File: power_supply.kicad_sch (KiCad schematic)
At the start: 0 parts

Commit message: add library from macbook
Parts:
- added U1: BQ25713RSNR, RSN0032B, symbol 2025-10-10_18-15-19:BQ25713RSNR
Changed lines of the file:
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@@
 	(generator_version "9.0")
 	(paper "A4")
+	(symbol
+		(lib_id "2025-10-10_18-15-19:BQ25713RSNR")
+		(at 91.44 86.36 0)
+		(unit 1)
+		(exclude_from_sim no)
+		(in_bom yes)
+		(on_board yes)
+		(dnp no)
+		(fields_autoplaced yes)
+		(property "Reference" "U1"
+			(at 91.44 30.48 0)
+			(effects
+				(font
+					(size 1.524 1.524)
+				)
+			)
+		)
+		(property "Value" "BQ25713RSNR"
+			(at 91.44 33.02 0)
+			(effects
+				(font
+					(size 1.524 1.524)
+				)
+			)
+		)
+		(property "Footprint" "RSN0032B"
+			(at 91.44 86.36 0)
+			(effects
+				(font
+					(size 1.27 1.27)
+					(italic yes)
+				)
+				(hide yes)
+			)
+		)
+		(property "Datasheet" "https://www.ti.com/lit/gpn/bq25713"
+			(at 91.44 86.36 0)
+			(effects
+				(font
+					(size 1.27 1.27)
+					(italic yes)
+				)
+				(hide yes)
+			)
+		)
+		(property "Description" ""
+			(at 91.44 86.36 0)
+			(effects
+				(font
+					(size 1.27 1.27)
+				)
+				(hide yes)
+			)
+		)
+		(pin "8"
+		)
+		(pin "9"
+		)
+		(pin "10"
+		)
+		(pin "27"
+		)
+		(pin "6"
+		)
+		(pin "28"
+		)
+		(pin "17"
+		)
+		(pin "18"
+		)
+		(pin "33"
+		)
+		(pin "32"
+		)
+		(pin "13"
+		)
+		(pin "12"
+		)
+		(pin "4"
+		)
+		(pin "5"
+		)
+		(pin "15"
+		)
+		(pin "14"
+		)
+		(pin "25"
+		)
+		(pin "23"
+		)
+		(pin "26"
+		)
+		(pin "24"
+		)
+		(pin "22"
+		)
+		(pin "21"
+		)
+		(pin "20"
+		)
+		(pin "19"
+		)
+		(pin "29"
+		)
+		(pin "30"
+		)
+		(pin "1"
+		)
+		(pin "11"
+		)
+		(pin "2"
+		)
+		(pin "3"
+		)
+		(pin "16"
+		)
+		(pin "7"
+		)
+		(pin "31"
+		)
+		(instances
+			(project ""
+				(path "/6a10ea30-147f-4e88-a5c3-bf0fd41178aa/90f8a919-9308-4e2d-9785-824a1b667211"
+					(reference "U1")
+					(unit 1)
+				)
+			)
+		)
+	)
 )

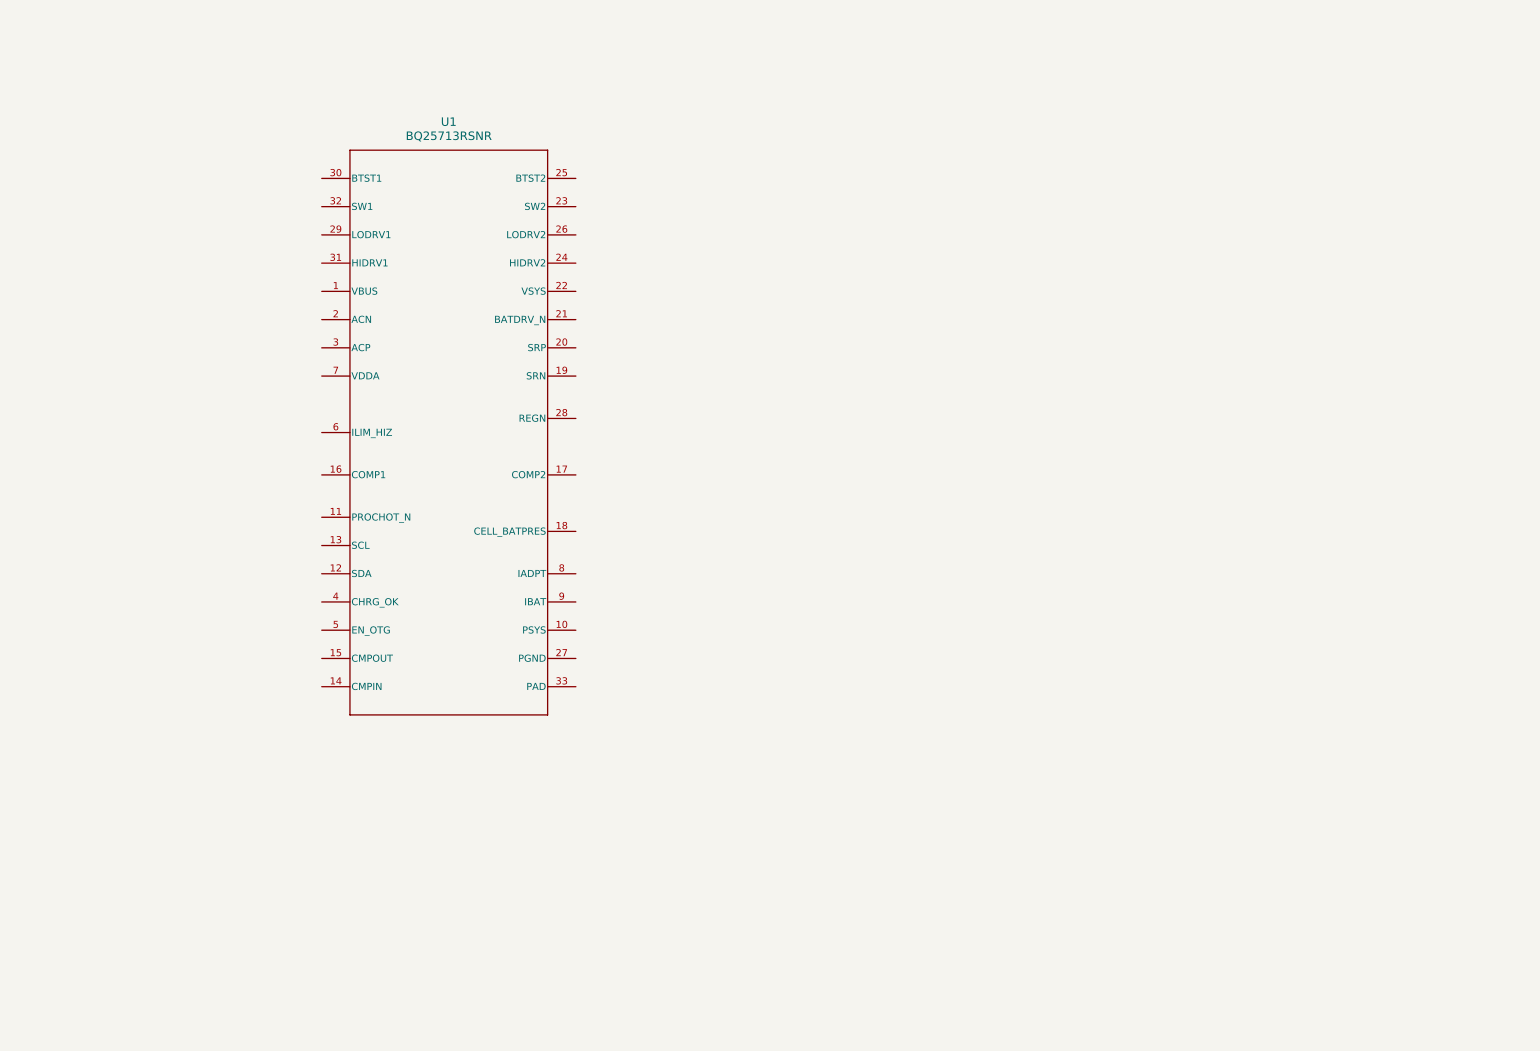
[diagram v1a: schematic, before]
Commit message: LTC4007 done, BQ7791 halfway implemented
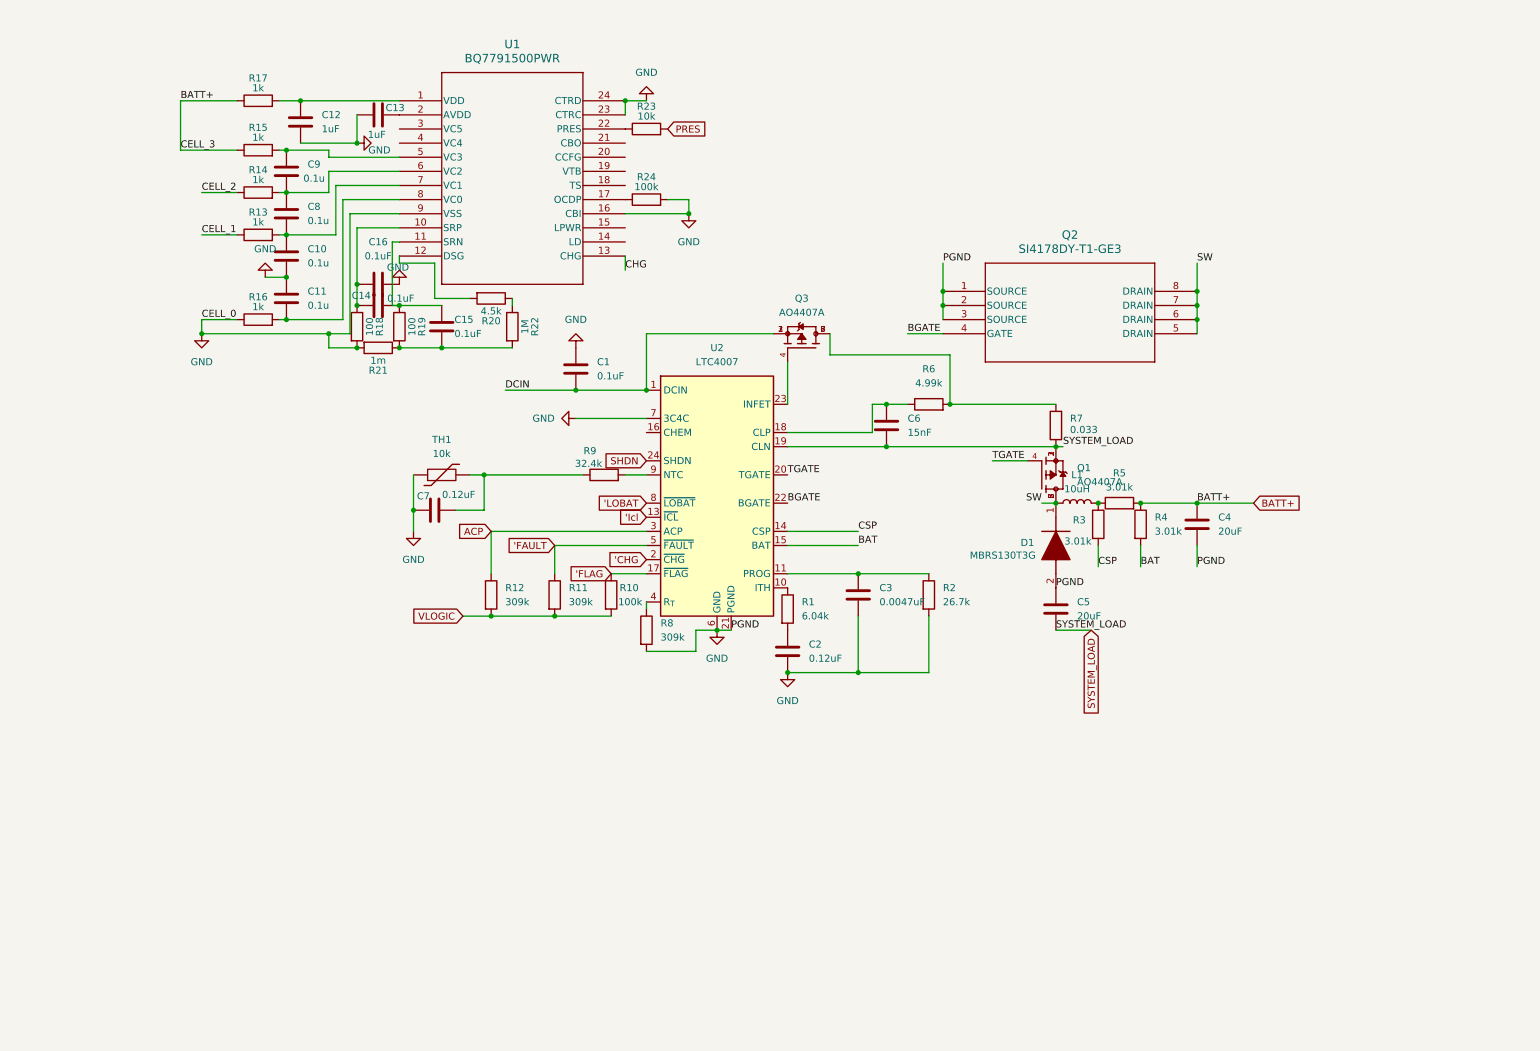
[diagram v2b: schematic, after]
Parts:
- removed U1: BQ25713RSNR, RSN0032B, symbol 2025-10-10_18-15-19:BQ25713RSNR
- added C1, C14, C15, C16: 0.1uF, Capacitor_SMD:C_0805_2012Metric_Pad1.18x1.45mm_HandSolder, symbol Device:C
- added C10, C11, C8, C9: 0.1u, Capacitor_SMD:C_0805_2012Metric_Pad1.18x1.45mm_HandSolder, symbol Device:C
- added C12, C13: 1uF, Capacitor_SMD:C_0805_2012Metric_Pad1.18x1.45mm_HandSolder, symbol Device:C
- added C2, C7: 0.12uF, Capacitor_SMD:C_0805_2012Metric_Pad1.18x1.45mm_HandSolder, symbol Device:C
- added C3: 0.0047uF, Capacitor_SMD:C_0805_2012Metric_Pad1.18x1.45mm_HandSolder, symbol Device:C
- added C4, C5: 20uF, Capacitor_SMD:C_0805_2012Metric_Pad1.18x1.45mm_HandSolder, symbol Device:C
- added C6: 15nF, Capacitor_SMD:C_0805_2012Metric_Pad1.18x1.45mm_HandSolder, symbol Device:C
- added D1: MBRS130T3G, DIOM5436X247N, symbol MBRS130T3G:MBRS130T3G
- added L1: 10uH, Inductor_SMD:L_0805_2012Metric_Pad1.05x1.20mm_HandSolder, symbol Device:L
- added Q1, Q3: AO4407A, AO4407A:SOIC127P600X175-8N, symbol AO4407A:AO4407A
- added Q2: SI4178DY-T1-GE3, SOIC_Y-T1-GE3_VIS, symbol SI4178DY-T1-GE3:SI4178DY-T1-GE3
- added R1: 6.04k, Resistor_SMD:R_0805_2012Metric_Pad1.20x1.40mm_HandSolder, symbol Device:R
- added R10, R24: 100k, Resistor_SMD:R_0805_2012Metric_Pad1.20x1.40mm_HandSolder, symbol Device:R
- added R11, R12, R8: 309k, Resistor_SMD:R_0805_2012Metric_Pad1.20x1.40mm_HandSolder, symbol Device:R
- added R13, R14, R15, R16, R17: 1k, Resistor_SMD:R_0805_2012Metric_Pad1.20x1.40mm_HandSolder, symbol Device:R
- added R18, R19: 100, Resistor_SMD:R_0805_2012Metric_Pad1.20x1.40mm_HandSolder, symbol Device:R
- added R2: 26.7k, Resistor_SMD:R_0805_2012Metric_Pad1.20x1.40mm_HandSolder, symbol Device:R
- added R20: 4.5k, Resistor_SMD:R_0805_2012Metric_Pad1.20x1.40mm_HandSolder, symbol Device:R
- added R21: 1m, Resistor_SMD:R_0805_2012Metric_Pad1.20x1.40mm_HandSolder, symbol Device:R
- added R22: 1M, Resistor_SMD:R_0805_2012Metric_Pad1.20x1.40mm_HandSolder, symbol Device:R
- added R23: 10k, Resistor_SMD:R_0805_2012Metric_Pad1.20x1.40mm_HandSolder, symbol Device:R
- added R3, R4, R5: 3.01k, Resistor_SMD:R_0805_2012Metric_Pad1.20x1.40mm_HandSolder, symbol Device:R
- added R6: 4.99k, Resistor_SMD:R_0805_2012Metric_Pad1.20x1.40mm_HandSolder, symbol Device:R
- added R7: 0.033, Resistor_SMD:R_0805_2012Metric_Pad1.20x1.40mm_HandSolder, symbol Device:R
- added R9: 32.4k, Resistor_SMD:R_0805_2012Metric_Pad1.20x1.40mm_HandSolder, symbol Device:R
- added TH1: 10k, Resistor_SMD:R_0805_2012Metric_Pad1.20x1.40mm_HandSolder, symbol Device:Thermistor
- added U1: BQ7791500PWR, PW24_TEX, symbol 2025-10-17_04-46-05:BQ7791500PWR
- added U2: LTC4007, Package_SO:SSOP-24_3.9x8.7mm_P0.635mm, symbol Battery_Management:LTC4007
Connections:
- new net: C12.1, R17.2, U1.1 (VDD)
- new net: C14.1, C16.1, R18.1, U1.10 (SRP)
- new net: C9.1, R15.2, U1.5 (VC3)
- new net: C8.1, C9.2, R14.2, U1.6 (VC2)
- new net: Q3.4, U2.23 (INFET)
- new net: Q3.5, Q3.6, Q3.7, Q3.8, R6.2, R7.2
- new net: R1.1, U2.10 (ITH)
- new net: C2.1, R1.2
- new net: L1.2, R3.1, R5.1
- new net: C15.2, R19.2, R21.1, R22.2
- new net: C6.1, R6.1, U2.18 (CLP)
- new net: C11.2, R16.2, U1.8 (VC0)
- new net: R8.1, U2.4 (R_{T})
- new net: C13.2, U1.2 (AVDD)
- new net: C7.2, R9.1, TH1.2
- new net: R9.2, U2.9 (NTC)
- new net: C14.2, C15.1, R19.1, U1.11 (SRN)
- new net: C10.1, C8.2, R13.2, U1.7 (VC1)
- new net: C3.1, R2.1, U2.11 (PROG)
- new net: R20.1, R22.1
- new net: R20.2, U1.12 (DSG)
- new net: R23.1, U1.22 (PRES)
- new net: R24.1, U1.17 (OCDP)
- new net 'CHG: U2.2 (~{CHG})
- new net 'FAULT: R11.1, U2.5 (~{FAULT})
- new net 'FLAG: R10.1, U2.17 (~{FLAG})
- new net 'Icl: U2.13 (~{ICL})
- new net 'LOBAT: U2.8 (~{LOBAT})
- new net ACP: R12.1, U2.3 (ACP)
- new net BAT: R4.2, U2.15 (BAT)
- new net BATT+: C4.1, R15.1, R17.1, R4.1, R5.2
- new net BGATE: Q2.4 (GATE), U2.22 (BGATE)
- new net CELL_1: R13.1
- new net CELL_2: R14.1
- new net CHG: U1.13 (CHG)
- new net CSP: R3.2, U2.14 (CSP)
- new net DCIN: C1.2, Q3.1, Q3.2, Q3.3, U2.1 (DCIN)
- new net GND: C1.1, C10.2, C11.1, C12.2, C13.1, C16.2, C2.2, C3.2, C4.2, C5.1, C7.1, D1.2 (A), Q2.1 (SOURCE), Q2.2 (SOURCE), Q2.3 (SOURCE), R16.1, R18.2, R2.2, R21.2, R24.2, R8.2, TH1.1, U1.16 (CBI), U1.23 (CTRC), U1.24 (CTRD), U1.9 (VSS), U2.21 (PGND), U2.6 (GND), U2.7 (3C4C)
- new net PRES: R23.2
- new net SHDN: U2.24 (SHDN)
- new net SW: D1.1 (K), L1.1, Q1.5, Q1.6, Q1.7, Q1.8, Q2.5 (DRAIN), Q2.6 (DRAIN), Q2.7 (DRAIN), Q2.8 (DRAIN)
- new net SYSTEM_LOAD: C5.2, C6.2, Q1.1, Q1.2, Q1.3, R7.1, U2.19 (CLN)
- new net TGATE: Q1.4, U2.20 (TGATE)
- new net VLOGIC: R10.2, R11.2, R12.2

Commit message: final commit before bed
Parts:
- added R25: 10k, Resistor_SMD:R_0805_2012Metric_Pad1.20x1.40mm_HandSolder, symbol Device:R
- added TH2: Thermistor_NTC, symbol Device:Thermistor_NTC
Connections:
- net GND: now also TH2.2
- net LD: now reaches U1.14 (LD)
- net at U1.18 (TS): now also R25.2, TH2.1
- net at U1.19 (VTB): now also R25.1
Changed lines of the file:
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@@
 	)
 	(junction
+		(at 130.81 41.91)
+		(diameter 0)
+		(color 0 0 0 0)
+	)
+	(junction
 		(at 74.93 63.5)
 		(diameter 0)
@@
 	(wire
 		(pts
+			(xy 139.7 46.99) (xy 134.62 46.99)
+		)
+		(stroke
+			(width 0)
+			(type default)
+		)
+	)
+	(wire
+		(pts
 			(xy 160.02 72.39) (xy 160.02 68.58)
 		)
@@
 	(wire
 		(pts
+			(xy 130.81 39.37) (xy 130.81 41.91)
+		)
+		(stroke
+			(width 0)
+			(type default)
+		)
+	)
+	(wire
+		(pts
 			(xy 123.19 26.67) (xy 127 26.67)
 		)
@@
 	(wire
 		(pts
+			(xy 138.43 41.91) (xy 139.7 41.91)
+		)
+		(stroke
+			(width 0)
+			(type default)
+		)
+	)
+	(wire
+		(pts
 			(xy 135.89 121.92) (xy 139.7 121.92)
 		)
@@
 	(wire
 		(pts
+			(xy 139.7 41.91) (xy 139.7 46.99)
+		)
+		(stroke
+			(width 0)
+			(type default)
+		)
+	)
+	(wire
+		(pts
 			(xy 82.55 54.61) (xy 82.55 55.88)
 		)
@@
 	(wire
 		(pts
+			(xy 123.19 41.91) (xy 130.81 41.91)
+		)
+		(stroke
+			(width 0)
+			(type default)
+		)
+	)
+	(wire
+		(pts
 			(xy 69.85 35.56) (xy 62.23 35.56)
 		)
@@
 		)
 	)
+	(label "LD"
+		(at 123.19 52.07 0)
+		(effects
+			(font
+				(size 1.27 1.27)
+			)
+			(justify left bottom)
+		)
+	)
 	(label "SW"
 		(at 226.06 55.88 0)
@@
 	)
 	(symbol
+		(lib_id "Device:Thermistor_NTC")
+		(at 134.62 41.91 90)
+		(unit 1)
+		(exclude_from_sim no)
+		(in_bom yes)
+		(on_board yes)
+		(dnp no)
+		(fields_autoplaced yes)
+		(property "Reference" "TH2"
+			(at 134.9375 35.56 90)
+			(effects
+				(font
+					(size 1.27 1.27)
+				)
+			)
+		)
+		(property "Value" "Thermistor_NTC"
+			(at 134.9375 38.1 90)
+			(effects
+				(font
+					(size 1.27 1.27)
+				)
+			)
+		)
+		(property "Footprint" ""
+			(at 133.35 41.91 0)
+			(effects
+				(font
+					(size 1.27 1.27)
+				)
+				(hide yes)
+			)
+		)
+		(property "Datasheet" "~"
+			(at 133.35 41.91 0)
+			(effects
+				(font
+					(size 1.27 1.27)
+				)
+				(hide yes)
+			)
+		)
+		(property "Description" "Temperature dependent resistor, negative temperature coefficient"
+			(at 134.62 41.91 0)
+			(effects
+				(font
+					(size 1.27 1.27)
+				)
+				(hide yes)
+			)
+		)
+		(pin "1"
+		)
+		(pin "2"
+		)
+		(instances
+			(project ""
+				(path "/6a10ea30-147f-4e88-a5c3-bf0fd41178aa/90f8a919-9308-4e2d-9785-824a1b667211"
+					(reference "TH2")
+					(unit 1)
+				)
+			)
+		)
+	)
+	(symbol
 		(lib_id "Device:R")
 		(at 208.28 102.87 0)
@@
 	)
 	(symbol
+		(lib_id "Device:R")
+		(at 127 39.37 90)
+		(unit 1)
+		(exclude_from_sim no)
+		(in_bom yes)
+		(on_board yes)
+		(dnp no)
+		(property "Reference" "R25"
+			(at 127 35.306 90)
+			(effects
+				(font
+					(size 1.27 1.27)
+				)
+			)
+		)
+		(property "Value" "10k"
+			(at 127 37.084 90)
+			(effects
+				(font
+					(size 1.27 1.27)
+				)
+			)
+		)
+		(property "Footprint" "Resistor_SMD:R_0805_2012Metric_Pad1.20x1.40mm_HandSolder"
+			(at 127 41.148 90)
+			(effects
+				(font
+					(size 1.27 1.27)
+				)
+				(hide yes)
+			)
+		)
+		(property "Datasheet" "~"
+			(at 127 39.37 0)
+			(effects
+				(font
+					(size 1.27 1.27)
+				)
+				(hide yes)
+			)
+		)
+		(property "Description" "Resistor"
+			(at 127 39.37 0)
+			(effects
+				(font
+					(size 1.27 1.27)
+				)
+				(hide yes)
+			)
+		)
+		(pin "1"
+		)
+		(pin "2"
+		)
+		(instances
+			(project "Strain Wave Motor Control Board"
+				(path "/6a10ea30-147f-4e88-a5c3-bf0fd41178aa/90f8a919-9308-4e2d-9785-824a1b667211"
+					(reference "R25")
+					(unit 1)
+				)
+			)
+		)
+	)
+	(symbol
 		(lib_id "Device:C")
 		(at 165.1 115.57 0)
@@
 		(dnp no)
 		(property "Reference" "R24"
-			(at 127 40.386 90)
+			(at 131.318 46.228 90)
 			(effects
 				(font
@@
 		)
 		(property "Value" "100k"
-			(at 127 42.164 90)
+			(at 127 44.45 90)
 			(effects
 				(font
